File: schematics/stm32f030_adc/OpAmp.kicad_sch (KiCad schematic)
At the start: 15 parts, among them U5 TL072

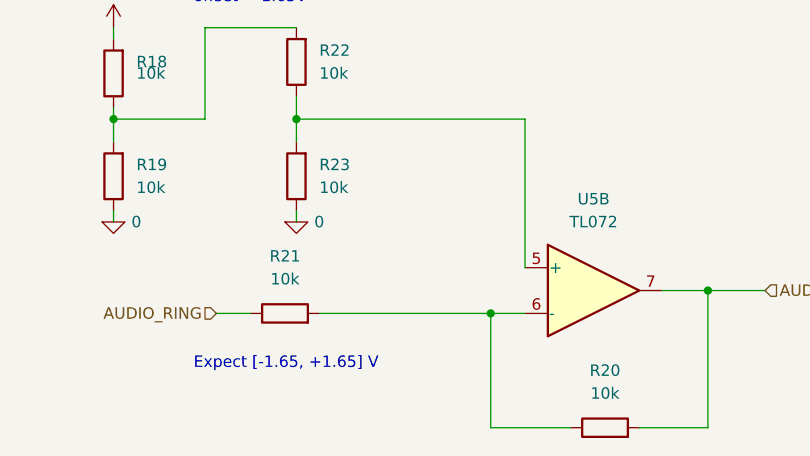
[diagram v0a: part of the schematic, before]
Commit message: [stm32f030_adc:OpAmp] Bug | Missing capacitor\
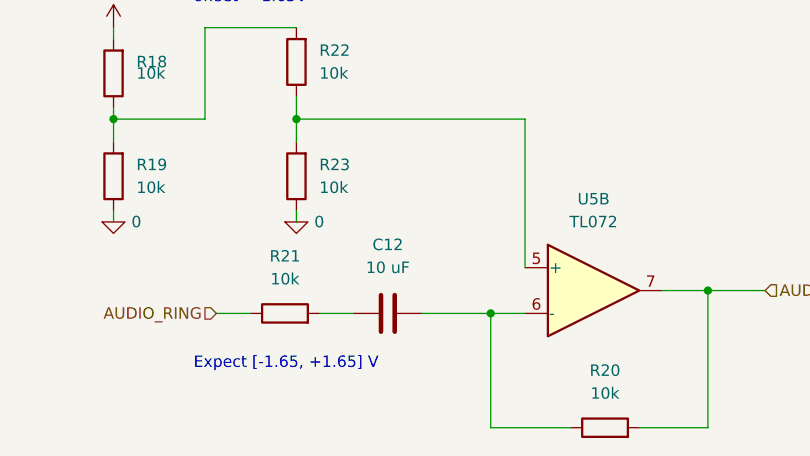
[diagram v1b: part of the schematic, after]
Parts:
- added C12: 10 uF, symbol Device:C
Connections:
- net at R20.1, U5.6 (-): now also C12.1; no longer R21.2
- new net: C12.2, R21.2
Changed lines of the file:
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@@
     (stroke (width 0) (type default))
   )
-  (wire (pts (xy 205.74 111.76) (xy 224.79 111.76))
+  (wire (pts (xy 205.74 111.76) (xy 209.55 111.76))
     (stroke (width 0) (type default))
   )
@@
   )
   (wire (pts (xy 82.55 88.9) (xy 82.55 78.74))
+    (stroke (width 0) (type default))
+  )
+  (wire (pts (xy 217.17 111.76) (xy 224.79 111.76))
     (stroke (width 0) (type default))
   )
@@
     (effects (font (size 1.27 1.27)) (justify right))
   )
+  (symbol (lib_id "Device:C") (at 213.36 111.76 270) (mirror x) (unit 1)
+    (in_bom yes) (on_board yes) (dnp no) (fields_autoplaced)
+    (property "Reference" "C12" (at 213.36 104.14 90)
+      (effects (font (size 1.27 1.27)))
+    )
+    (property "Value" "10 uF" (at 213.36 106.68 90)
+      (effects (font (size 1.27 1.27)))
+    )
+    (property "Footprint" "" (at 209.55 110.7948 0)
+      (effects (font (size 1.27 1.27)) hide)
+    )
+    (property "Datasheet" "~" (at 213.36 111.76 0)
+      (effects (font (size 1.27 1.27)) hide)
+    )
+    (pin "1")
+    (pin "2")
+    (instances
+      (project "stm32f030_adc"
+        (path "/85629656-c73b-4e1f-b8e8-4366f4b01266/b4185304-bcce-4cb1-98f3-8bffc8e76c1e"
+          (reference "C12") (unit 1)
+        )
+      )
+    )
+  )
   (symbol (lib_id "Simulation_SPICE:0") (at 92.71 100.33 0) (unit 1)
